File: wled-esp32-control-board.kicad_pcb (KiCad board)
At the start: 4 copper layers, 64.9 x 39.5 mm, 53 parts, among them J101 Conn_01x03, J102 Conn_01x03, J103 Conn_01x03, J104 Conn_01x03, J105 Conn_02x03_Odd_Even, J201 USB_C_Receptacle_USB2.0, Q401 MMDT3904, SW101 SW_SPDT, SW103 SW_Push, SW105 SW_Push, U101 74AHCT1G125, U102 74AHCT1G125, U103 ESP32-WROOM-32, U104 74AHCT1G125, U105 74AHCT1G125, U106 TSOP382xx, U301 XC6220B331MR-G, U401 CP2102-GMR

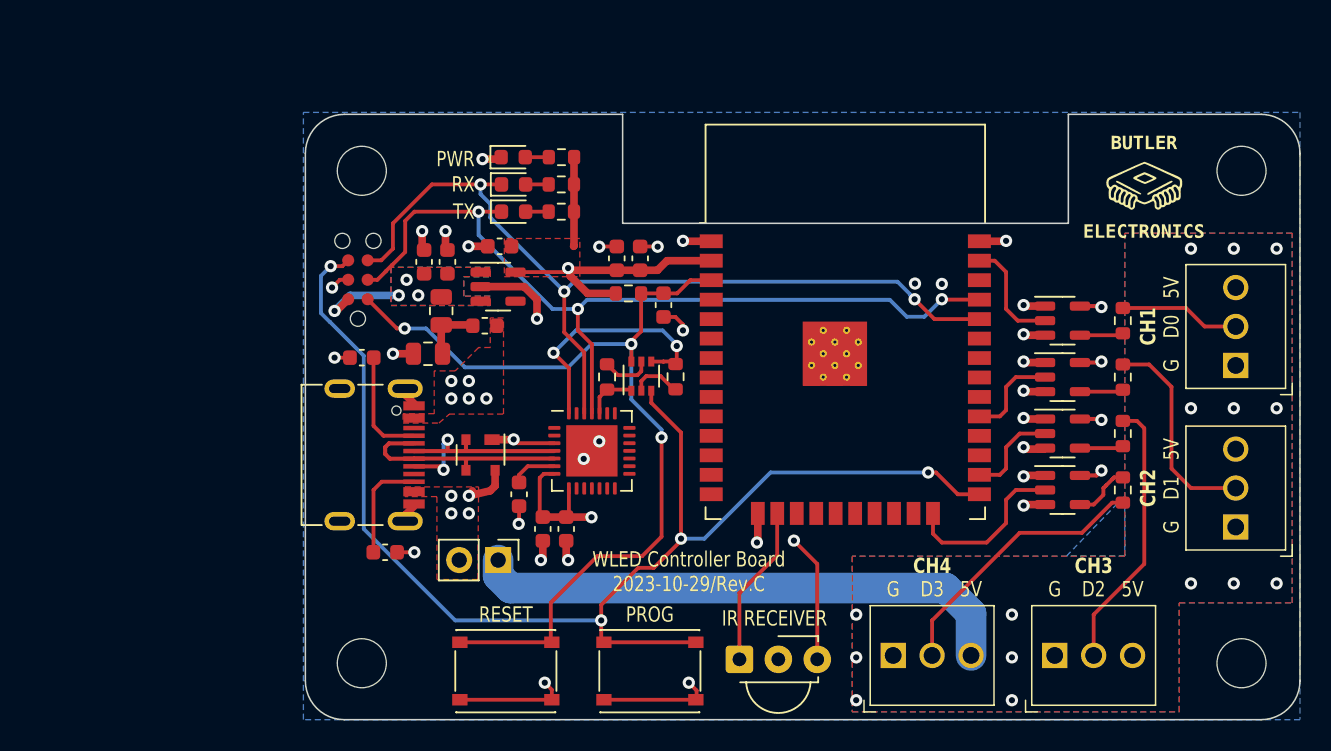
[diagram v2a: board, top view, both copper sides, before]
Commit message: update design to replace CP2102 and LDO
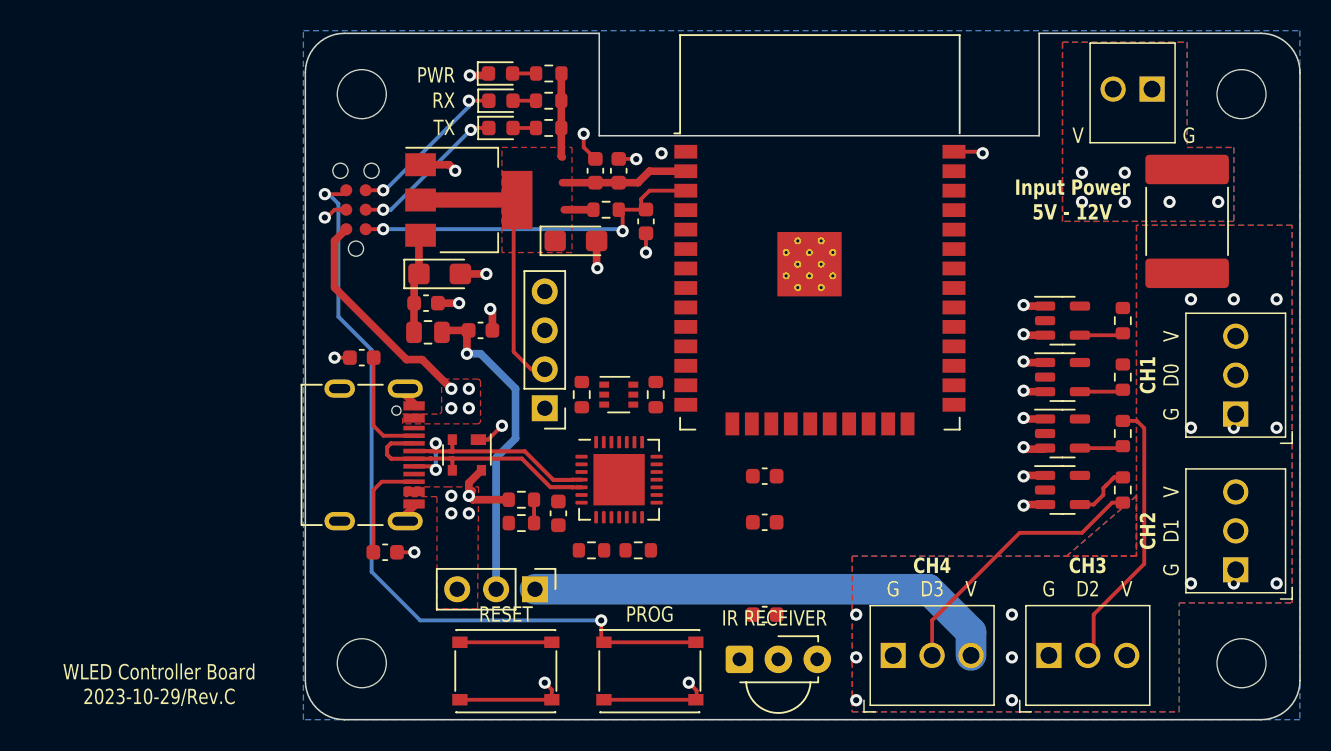
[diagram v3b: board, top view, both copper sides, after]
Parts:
- removed C201: 10uF, Capacitor_SMD:C_0805_2012Metric
- removed C202: 100nF, Capacitor_SMD:C_0603_1608Metric
- removed F201: Polyfuse_Small, Fuse:Fuse_0603_1608Metric
- removed FB201: FerriteBead_Small, Resistor_SMD:R_0805_2012Metric
- added C303: 10uF, Capacitor_SMD:C_0603_1608Metric, F.Cu at (109.3, 82.5)
- added C304: 100nF, Capacitor_SMD:C_0603_1608Metric, F.Cu at (105.8, 80.8)
- added C404: 100nF, Capacitor_SMD:C_0603_1608Metric, F.Cu at (127.9, 101.1)
- added F101: Polyfuse_Small, Fuse:Fuse_2920_7451Metric, F.Cu at (155.4, 75.4)
- added FB301: FerriteBead_Small, Resistor_SMD:R_0805_2012Metric, F.Cu at (105.9, 82.7)
- added J106: Screw_Terminal_01x02, User_Footprint:397730002, F.Cu at (153.2, 66.8)
- added OLED101: OLED_I2C, User_Footprint:OLED_128x32_I2C_4pins, F.Cu at (131.1, 83.8)
- added R403: 22K1, Resistor_SMD:R_0603_1608Metric, F.Cu at (112.0, 93.6)
- added R404: 47K5, Resistor_SMD:R_0603_1608Metric, F.Cu at (112.0, 95.1)
- added R405: 10K, Resistor_SMD:R_0603_1608Metric, F.Cu at (120.8, 86.7)
- added R408: 10K, Resistor_SMD:R_0603_1608Metric, F.Cu at (119.6, 96.9)
- C301: value 22uF -> 10uF; footprint Capacitor_SMD:C_0603_1608Metric -> Capacitor_Tantalum_SMD:CP_EIA-3216-10_Kemet-I
- C302: value 4.7uF -> 10uF; footprint Capacitor_SMD:C_0603_1608Metric -> Capacitor_Tantalum_SMD:CP_EIA-3216-10_Kemet-I
- C402: value 1uF -> 4.7uF
- C403: value 100nF -> 4.7uF
- G***: moved to B.Cu
- R401: value 10K -> 1K
- SW101: footprint Connector_PinHeader_2.54mm:PinHeader_1x02_P2.54mm_Vertical -> Connector_PinHeader_2.54mm:PinHeader_1x03_P2.54mm_Vertical
- U301: value XC6220B331MR-G -> LM1117MP-3.3; footprint Package_TO_SOT_SMD:SOT-23-5 -> Package_TO_SOT_SMD:SOT-223-3_TabPin2
- U401: value CP2102-GMR -> CP2102N-Axx-xQFN28
- moved C401 16.1 mm to (127.9, 92.1), turned to 0 degrees
- moved C402 14.5 mm to (127.9, 95.1), turned to 0 degrees
- moved G*** 14.1 mm to (138.7, 75.2), turned to 180 degrees
- moved R401 12.6 mm to (116.6, 96.9), turned to 0 degrees
- moved U103 6.07 mm to (131.5, 79.1)
- moved U301 5.97 mm to (108.6, 74.0)
- moved C101 5.88 mm to (116.8, 72.1)
- moved C102 5.88 mm to (118.4, 72.1)
- moved R101 5.65 mm to (117.5, 74.7)
- moved C104 5.58 mm to (120.1, 75.4)
- moved LED102 5.52 mm to (110.7, 67.6)
- moved R105 5.52 mm to (113.8, 67.6)
- moved LED103 5.52 mm to (110.7, 65.8)
- moved LED101 5.52 mm to (110.7, 69.3)
- moved R104 5.52 mm to (113.8, 69.3)
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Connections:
- net /USB-TTL-AutoProgram/D_N renamed /CP2102N-AutoProgram/D_N
- net /USB-TTL-AutoProgram/D_P renamed /CP2102N-AutoProgram/D_P
- C301 pad 1: GND -> Net-(U301-VI)
- C301 pad 2: +5V -> GND
- C401 pad 1: Net-(U401-VDD) -> /CP2102N-AutoProgram/VDD
- C402 pad 1: +5V -> /CP2102N-AutoProgram/VDD
- C403 pad 1: +5V -> /CP2102N-AutoProgram/VREGIN
- D201 pad 4: VCC -> +5V
- J201 pad A4: VCC -> +5V
- J201 pad A9: VCC -> +5V
- J201 pad B4: VCC -> +5V
- J201 pad B9: VCC -> +5V
- Q401 pad 1: /USB-TTL-AutoProgram/RTS -> /CP2102N-AutoProgram/RTS
- Q401 pad 4: /USB-TTL-AutoProgram/DTR -> /CP2102N-AutoProgram/DTR
- R401 pad 1: Net-(Q401A-B1) -> /CP2102N-AutoProgram/VDD
- R401 pad 2: /USB-TTL-AutoProgram/DTR -> Net-(U401-~{RST})
- R402 pad 1: Net-(Q401B-B2) -> Net-(Q401A-B1)
- R402 pad 2: /USB-TTL-AutoProgram/RTS -> /CP2102N-AutoProgram/DTR
- SW101 pad 2: VCC -> /LDO/VIN
- U101 pad 5: +5V -> /LED_PWR
- U102 pad 5: +5V -> /LED_PWR
- U103 pad 33: unconnected-(U103-IO21-Pad33) -> /SDA
- U103 pad 36: unconnected-(U103-IO22-Pad36) -> /SCL
- U104 pad 5: +5V -> /LED_PWR
- U105 pad 5: +5V -> /LED_PWR
- U301 pad 1: +5V -> GND
- U301 pad 2: GND -> +3.3V
- U301 pad 3: +5V -> Net-(U301-VI)
- U401 pad 11: unconnected-(U401-~{SUSPEND}-Pad11) -> Net-(U401-~{SUSPEND})
- U401 pad 24: /USB-TTL-AutoProgram/RTS -> /CP2102N-AutoProgram/RTS
- U401 pad 28: /USB-TTL-AutoProgram/DTR -> /CP2102N-AutoProgram/DTR
- U401 pad 6: Net-(U401-VDD) -> /CP2102N-AutoProgram/VDD
- U401 pad 7: +5V -> /CP2102N-AutoProgram/VREGIN
- U401 pad 8: +5V -> Net-(U401-VBUS)
- U401 pad 9: unconnected-(U401-~{RST}-Pad9) -> Net-(U401-~{RST})
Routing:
- net +5V: track 91.4 -> 32.5 mm, vias 9 -> 8
- net /ESP_RX: track 57.9 -> 10.7 mm, vias 3 -> 2
- net /ESP_TX: track 56.3 -> 10.2 mm, vias 3 -> 2
- net /IO0: track 85.7 -> 51.4 mm, vias 4 -> 2
- net /EN: track 60.4 -> 29.6 mm, vias 3 -> 2
- net +3.3V: track 58.1 -> 34.4 mm, vias 2 -> 0
- net /LDO/VIN: track 0.00 -> 21.1 mm, vias 0 -> 1
- net VCC: track 16.7 -> 0.00 mm, vias 9 -> 0
- net /USB-TTL-AutoProgram/DTR: track 16.4 -> 0.00 mm, vias 2 -> 0
- net Net-(J102-Pin_2): track 13.8 -> 0.00 mm
- net /LED3: track 11.2 -> 0.00 mm
- net GND: track 61.2 -> 50.4 mm, vias 33 -> 25
- net /IR_RECV: track 10.5 -> 0.00 mm
- net Net-(J101-Pin_2): track 7.87 -> 0.00 mm
- net /LED0: track 7.32 -> 0.00 mm
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- added copper zone on B.Cu, net Net-(J106-Pin_2)
- added copper zone on F.Cu, net Net-(J106-Pin_2)
- added copper zone on In2.Cu, net Net-(J106-Pin_2)
- removed copper zone on B.Cu, net +5V
- removed copper zone on F.Cu, net VCC
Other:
- board size 64.9 x 39.5 mm -> 64.9 x 44.8 mm
- board text added: "Input Power 5V - 12V"
- board text added: "V"
- board text removed: "5V"

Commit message: refactor to accept 12V power
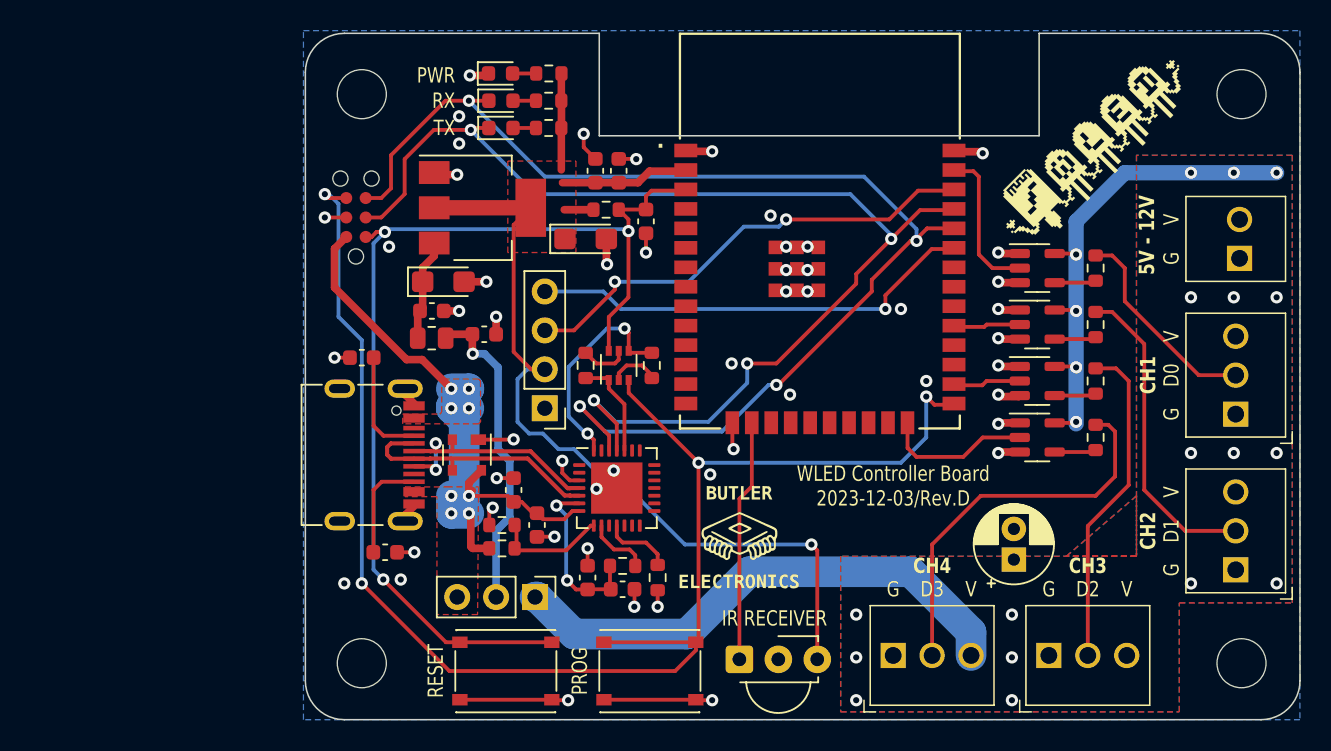
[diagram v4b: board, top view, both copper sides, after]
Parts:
- removed F101: Polyfuse_Small, Fuse:Fuse_2920_7451Metric
- added C103: 100uF, Capacitor_THT:CP_Radial_D5.0mm_P2.00mm, F.Cu at (144.1, 97.5)
- added G***: LOGO, LOGO, F.Cu at (149.4, 70.6)
- G***: moved to F.Cu
- U103: footprint User_Footprint:ESP32-WROOM-32 -> User_Footprint:ESP32­-WROOM­-32E
- moved G*** 24.3 mm to (126.2, 96.0), turned to 0 degrees
- moved C404 16.0 mm to (113.0, 95.2), turned to -90 degrees
- moved C401 13.3 mm to (116.3, 98.7), turned to 90 degrees
- moved J106 12.4 mm to (158.9, 77.9), turned to 90 degrees
- moved C402 10.2 mm to (118.6, 99.4)
- moved R402 4.95 mm to (120.5, 84.8)
- moved R405 4.95 mm to (116.2, 84.8), turned to -90 degrees
- moved R102 3.86 mm to (149.5, 78.5)
- moved R103 3.86 mm to (149.5, 82.2)
- moved R106 3.86 mm to (149.5, 85.9)
- moved R108 3.86 mm to (149.5, 89.5), turned to 90 degrees
- moved U101 3.81 mm to (145.7, 78.5)
- moved U102 3.81 mm to (145.7, 82.2)
- moved U104 3.81 mm to (145.7, 85.9)
- moved U105 3.81 mm to (145.7, 89.5)
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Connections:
- C403 pad 1: /CP2102N-AutoProgram/VREGIN -> +5V
- C404 pad 1: /CP2102N-AutoProgram/VREGIN -> +5V
- J106 pad 2: Net-(J106-Pin_2) -> /LED_PWR
- U401 pad 7: /CP2102N-AutoProgram/VREGIN -> +5V
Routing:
- net /ESP_RX: track 10.7 -> 80.2 mm, vias 2 -> 4
- net /ESP_TX: track 10.2 -> 77.1 mm, vias 2 -> 4
- net /IO0: track 51.4 -> 98.6 mm, vias 2 -> 4
- net /EN: track 29.6 -> 68.8 mm, vias 2 -> 3
- net /LED_PWR: track 31.1 -> 67.6 mm, vias 15 -> 21
- net +3.3V: track 34.4 -> 70.2 mm, vias 0 -> 1
- net /SCL: track 0.00 -> 30.8 mm, vias 0 -> 2
- net /SDA: track 0.00 -> 29.3 mm, vias 0 -> 1
- net Net-(J102-Pin_2): track 0.00 -> 20.6 mm
- net /IR_RECV: track 0.00 -> 15.7 mm
- net /CP2102N-AutoProgram/DTR: track 0.00 -> 14.0 mm, vias 0 -> 2
- net Net-(J101-Pin_2): track 0.00 -> 13.6 mm
- net /CP2102N-AutoProgram/VDD: track 0.00 -> 11.4 mm, vias 0 -> 2
- net GND: track 50.4 -> 60.5 mm, vias 25 -> 52
- net /LED0: track 0.00 -> 9.89 mm
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- removed copper zone on B.Cu, net Net-(J106-Pin_2)
- removed copper zone on F.Cu, net Net-(J106-Pin_2)
- removed copper zone on In2.Cu, net Net-(J106-Pin_2)
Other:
- board text added: "0"
- board text added: "0 mm"
- board text added: "0.0152 mm"
- board text added: "0.02"
- board text added: "0.02032 mm"
- board text added: "0.035 mm"
- board text added: "0.0900 mm / 0.0900 mm"
- board text added: "0.2000 mm"
- board text added: "0.2104 mm"
- board text added: "1"
- board text added: "1.065 mm"
- board text added: "1.6268 mm"
- board text added: "3.3"
- board text added: "4"
- board text added: "4.6"
- board text added: "5V - 12V"
- board text added: "64.8970 mm x 44.7830 mm"
- board text added: "B.Cu"
- board text added: "B.Mask"
- board text added: "B.Paste"
- board text added: "B.Silkscreen"
- board text added: "BOARD CHARACTERISTICS"
- board text added: "Black"
- board text added: "Board Thickness:"
- board text added: "Board overall dimensions:"
- board text added: "Bottom Silk Screen"
- board text added: "Bottom Solder Mask"
- board text added: "Bottom Solder Paste"
- board text added: "Castellated pads:"
- board text added: "Color"
- board text added: "Copper Finish:"
- board text added: "Copper Layer Count:"
- board text added: "Design by Dr. Joshua Butler"
- board text added: "Dielectric"
- board text added: "Edge card connectors:"
- board text added: "Epsilon R"
- board text added: "External Fuse is Required"
- board text added: "F.Cu"
- board text added: "F.Mask"
- board text added: "F.Paste"
- board text added: "F.Silkscreen"
- board text added: "FR4"
- board text added: "FR4 natural"
- board text added: "HAL SnPb"
- board text added: "Impedance Control:"
- board text added: "In1.Cu"
- board text added: "In2.Cu"
- board text added: "Layer Name"
- board text added: "Loss Tangent"
- board text added: "Material"
- board text added: "Min hole diameter:"
- board text added: "Min track/spacing:"
- board text added: "No"
- board text added: "Not specified"
- board text added: "Plated Board Edge:"
- board text added: "Thickness (mm)"
- board text added: "Top Silk Screen"
- board text added: "Top Solder Mask"
- board text added: "Top Solder Paste"
- board text added: "Type"
- board text added: "White"
- board text added: "copper"
- board text added: "core"
- board text added: "prepreg"
- board text removed: "Input Power 5V - 12V"
